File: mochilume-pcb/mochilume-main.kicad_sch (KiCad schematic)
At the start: 28 parts, among them U1 llcc68_custom_module

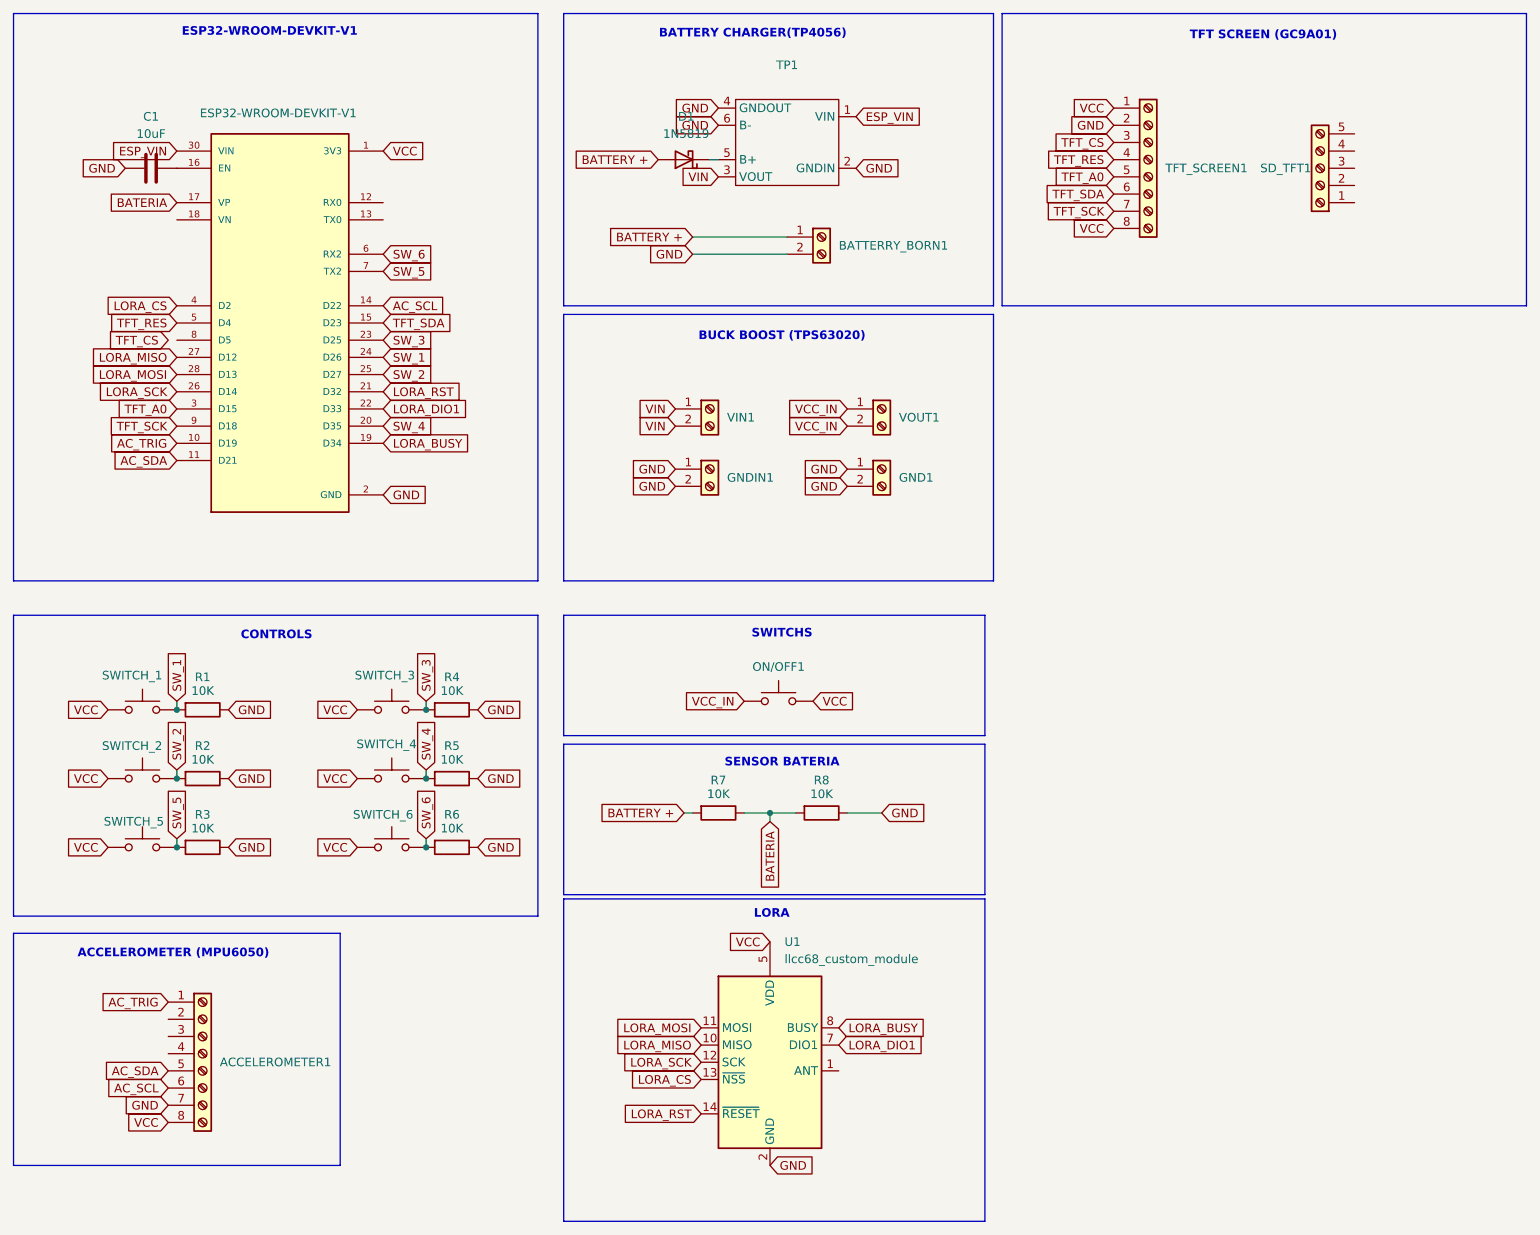
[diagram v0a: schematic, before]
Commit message: feat main pcb: add vias tracking to main pcb
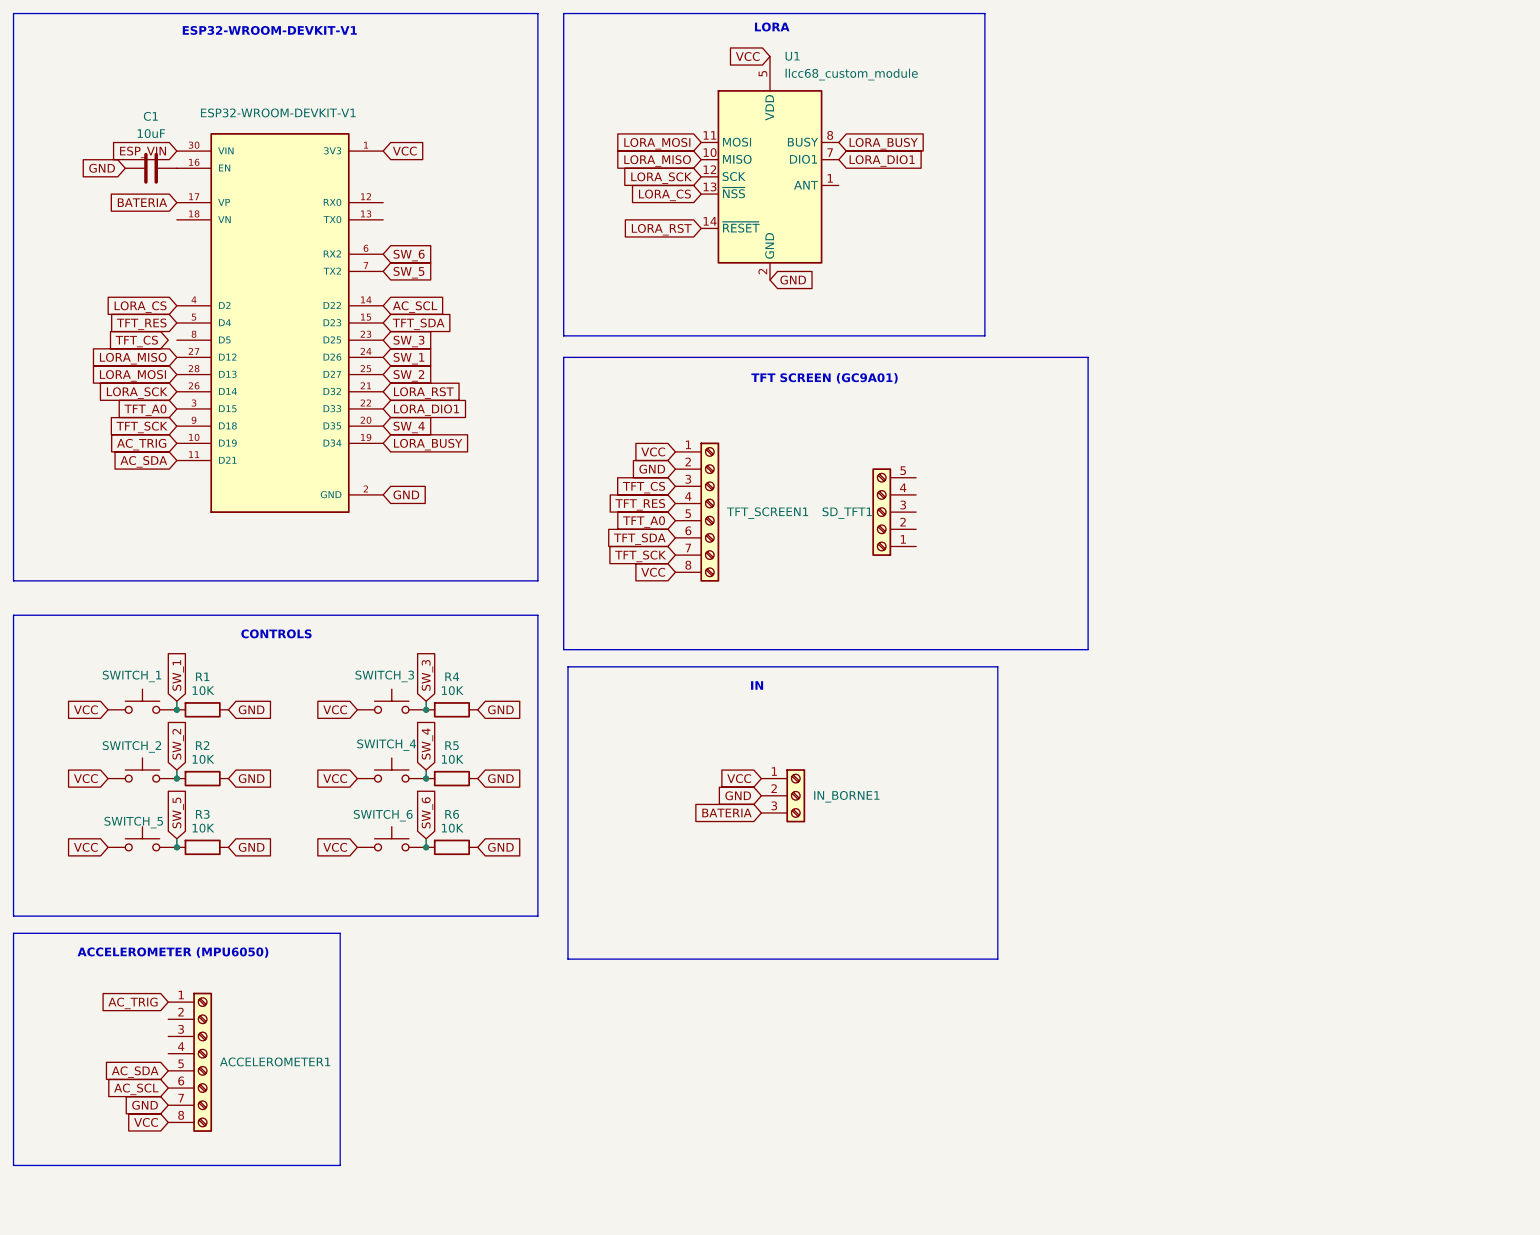
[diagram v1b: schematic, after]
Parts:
- removed BATTERRY_BORN1: (no value), TerminalBlock_Phoenix:TerminalBlock_Phoenix_MKDS-1,5-2-5.08_1x02_P5.08mm_Horizontal, symbol Connector:Screw_Terminal_01x02
- removed D1: 1N5819, Diode_THT:D_DO-41_SOD81_P10.16mm_Horizontal, symbol Diode:1N5819
- removed GND1, GNDIN1, VIN1, VOUT1: (no value), Connector_PinHeader_2.54mm:PinHeader_1x02_P2.54mm_Vertical, symbol Connector:Screw_Terminal_01x02
- removed ON/OFF1: (no value), TerminalBlock_Phoenix:TerminalBlock_Phoenix_MKDS-1,5-2-5.08_1x02_P5.08mm_Horizontal, symbol Switch:SW_Push
- removed R7, R8: 10K, Resistor_THT:R_Axial_DIN0309_L9.0mm_D3.2mm_P15.24mm_Horizontal, symbol Device:R
- removed TP1: (no value), Library:TP4056-18650, symbol teste_lib_kicad:TP4056
- added IN_BORNE1: Screw_Terminal_01x03, TerminalBlock:TerminalBlock_MaiXu_MX126-5.0-03P_1x03_P5.00mm, symbol Connector:Screw_Terminal_01x03
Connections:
- net BATERIA: now also IN_BORNE1.3 (Pin_3)
- net GND: now also IN_BORNE1.2 (Pin_2)
- net VCC: now also IN_BORNE1.1 (Pin_1)
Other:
- note added: "IN"
- note removed: "BATTERY CHARGER(TP4056)"
- note removed: "BUCK BOOST (TPS63020)"
- note removed: "SENSOR BATERIA"
- note removed: "SWITCHS"
- moved on the sheet: SD_TFT1, TFT_SCREEN1, U1

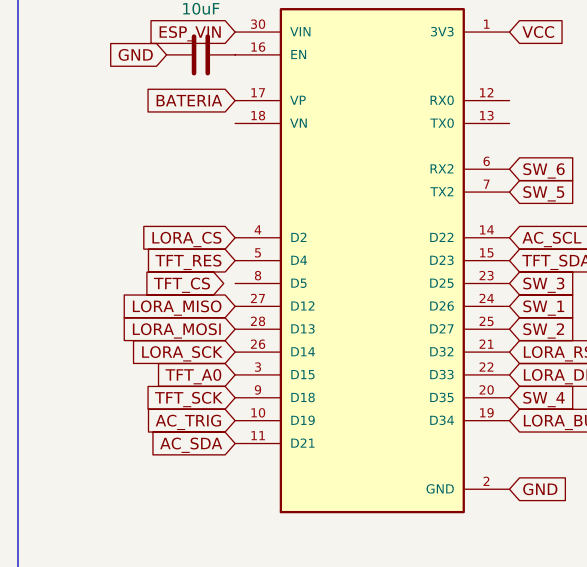
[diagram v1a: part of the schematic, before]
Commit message: fix: unconnected via between tft_cs and esp 32 pin 8
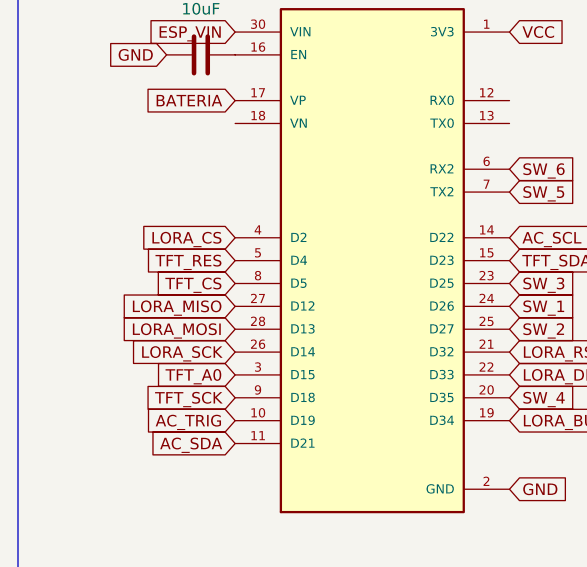
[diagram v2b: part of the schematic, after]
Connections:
- net TFT_CS: now also ESP32-WROOM-DEVKIT-V1.8 (D5)
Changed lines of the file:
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@@
-		)
-	)
-	(global_label "TFT_CS"
-		(shape input)
-		(at 40.64 67.31 180)
-		(fields_autoplaced yes)
-		(effects
-			(font
-				(size 1.27 1.27)
-			)
-			(justify right)
-		)
-		(property "Intersheetrefs" "${INTERSHEET_REFS}"
-			(at 31.1839 67.31 0)
-			(hide yes)
-			(show_name no)
-			(do_not_autoplace no)
-			(effects
-				(font
-					(size 1.27 1.27)
-				)
-				(justify right)
-			)
 		)
 	)
@@
 			(hide yes)
 			(show_name no)
+			(do_not_autoplace no)
+			(effects
+				(font
+					(size 1.27 1.27)
+				)
+				(justify right)
+			)
+		)
+	)
+	(global_label "TFT_CS"
+		(shape input)
+		(at 41.91 67.31 180)
+		(fields_autoplaced yes)
+		(effects
+			(font
+				(size 1.27 1.27)
+			)
+			(justify right)
+		)
+		(property "Intersheetrefs" "${INTERSHEET_REFS}"
+			(at 32.4539 67.31 0)
+			(hide yes)
+			(show_name no)
